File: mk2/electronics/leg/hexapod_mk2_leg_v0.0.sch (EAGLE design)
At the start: 5 parts

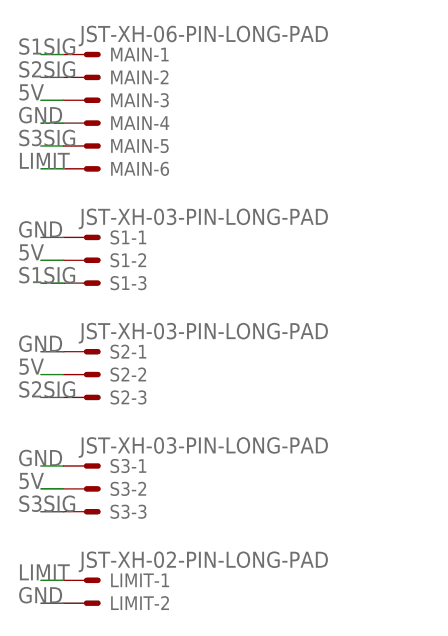
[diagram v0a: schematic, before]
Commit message: servo decoupling caps
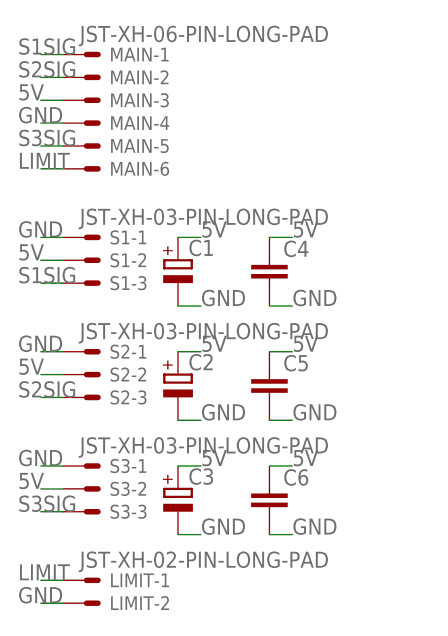
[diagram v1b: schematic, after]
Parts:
- added C1, C2, C3: (no value), rcl:CPOL-EUE2-5
- added C4, C5, C6: (no value), rcl:C-EUC1206
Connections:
- net 5V: now also C1.+, C2.+, C3.+, C4.1, C5.1, C6.1
- net GND: now also C1.-, C2.-, C3.-, C4.2, C5.2, C6.2
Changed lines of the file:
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@@
 <part name="LIMIT" library="Rembrandt Electronics - JST XH Connectors v1-0" deviceset="JST-XH-02-PIN" device="-LONG-PAD"/>
 <part name="MAIN" library="Rembrandt Electronics - JST XH Connectors v1-0" deviceset="JST-XH-06-PIN" device="-LONG-PAD"/>
+<part name="C1" library="rcl" library_urn="urn:adsk.eagle:library:334" deviceset="CPOL-EU" device="E2-5" package3d_urn="urn:adsk.eagle:package:23346/2"/>
+<part name="C2" library="rcl" library_urn="urn:adsk.eagle:library:334" deviceset="CPOL-EU" device="E2-5" package3d_urn="urn:adsk.eagle:package:23346/2"/>
+<part name="C3" library="rcl" library_urn="urn:adsk.eagle:library:334" deviceset="CPOL-EU" device="E2-5" package3d_urn="urn:adsk.eagle:package:23346/2"/>
+<part name="C4" library="rcl" library_urn="urn:adsk.eagle:library:334" deviceset="C-EU" device="C1206" package3d_urn="urn:adsk.eagle:package:23618/2"/>
+<part name="C5" library="rcl" library_urn="urn:adsk.eagle:library:334" deviceset="C-EU" device="C1206" package3d_urn="urn:adsk.eagle:package:23618/2"/>
+<part name="C6" library="rcl" library_urn="urn:adsk.eagle:library:334" deviceset="C-EU" device="C1206" package3d_urn="urn:adsk.eagle:package:23618/2"/>
 </parts>
 <sheets>
@@
 <attribute name="NAME" x="35.56" y="65.278" size="1.524" layer="95"/>
 </instance>
+<instance part="C1" gate="G$1" x="43.18" y="55.88" smashed="yes">
+<attribute name="NAME" x="44.323" y="56.3626" size="1.778" layer="95"/>
+<attribute name="VALUE" x="44.323" y="51.2826" size="1.778" layer="96"/>
+</instance>
+<instance part="C2" gate="G$1" x="43.18" y="43.18" smashed="yes">
+<attribute name="NAME" x="44.323" y="43.6626" size="1.778" layer="95"/>
+<attribute name="VALUE" x="44.323" y="38.5826" size="1.778" layer="96"/>
+</instance>
+<instance part="C3" gate="G$1" x="43.18" y="30.48" smashed="yes">
+<attribute name="NAME" x="44.323" y="30.9626" size="1.778" layer="95"/>
+<attribute name="VALUE" x="44.323" y="25.8826" size="1.778" layer="96"/>
+</instance>
+<instance part="C4" gate="G$1" x="53.34" y="55.88" smashed="yes">
+<attribute name="NAME" x="54.864" y="56.261" size="1.778" layer="95"/>
+<attribute name="VALUE" x="54.864" y="51.181" size="1.778" layer="96"/>
+</instance>
+<instance part="C5" gate="G$1" x="53.34" y="43.18" smashed="yes">
+<attribute name="NAME" x="54.864" y="43.561" size="1.778" layer="95"/>
+<attribute name="VALUE" x="54.864" y="38.481" size="1.778" layer="96"/>
+</instance>
+<instance part="C6" gate="G$1" x="53.34" y="30.48" smashed="yes">
+<attribute name="NAME" x="54.864" y="30.861" size="1.778" layer="95"/>
+<attribute name="VALUE" x="54.864" y="25.781" size="1.778" layer="96"/>
+</instance>
 </instances>
 <busses>
@@
 <label x="25.4" y="73.66" size="1.778" layer="95"/>
 </segment>
+<segment>
+<pinref part="C3" gate="G$1" pin="+"/>
+<wire x1="43.18" y1="33.02" x2="45.72" y2="33.02" width="0.1524" layer="91"/>
+<label x="45.72" y="33.02" size="1.778" layer="95"/>
+</segment>
+<segment>
+<pinref part="C2" gate="G$1" pin="+"/>
+<wire x1="43.18" y1="45.72" x2="45.72" y2="45.72" width="0.1524" layer="91"/>
+<label x="45.72" y="45.72" size="1.778" layer="95"/>
+</segment>
+<segment>
+<pinref part="C1" gate="G$1" pin="+"/>
+<wire x1="43.18" y1="58.42" x2="45.72" y2="58.42" width="0.1524" layer="91"/>
+<label x="45.72" y="58.42" size="1.778" layer="95"/>
+</segment>
+<segment>
+<pinref part="C4" gate="G$1" pin="1"/>
+<wire x1="53.34" y1="58.42" x2="55.88" y2="58.42" width="0.1524" layer="91"/>
+<label x="55.88" y="58.42" size="1.778" layer="95"/>
+</segment>
+<segment>
+<pinref part="C5" gate="G$1" pin="1"/>
+<wire x1="53.34" y1="45.72" x2="55.88" y2="45.72" width="0.1524" layer="91"/>
+<label x="55.88" y="45.72" size="1.778" layer="95"/>
+</segment>
+<segment>
+<pinref part="C6" gate="G$1" pin="1"/>
+<wire x1="53.34" y1="33.02" x2="55.88" y2="33.02" width="0.1524" layer="91"/>
+<label x="55.88" y="33.02" size="1.778" layer="95"/>
+</segment>
 </net>
 <net name="GND" class="0">
@@
 <label x="25.4" y="71.12" size="1.778" layer="95"/>
 </segment>
+<segment>
+<pinref part="C3" gate="G$1" pin="-"/>
+<wire x1="43.18" y1="25.4" x2="45.72" y2="25.4" width="0.1524" layer="91"/>
+<label x="45.72" y="25.4" size="1.778" layer="95"/>
+</segment>
+<segment>
+<pinref part="C2" gate="G$1" pin="-"/>
+<wire x1="43.18" y1="38.1" x2="45.72" y2="38.1" width="0.1524" layer="91"/>
+<label x="45.72" y="38.1" size="1.778" layer="95"/>
+</segment>
+<segment>
+<pinref part="C1" gate="G$1" pin="-"/>
+<wire x1="43.18" y1="50.8" x2="45.72" y2="50.8" width="0.1524" layer="91"/>
+<label x="45.72" y="50.8" size="1.778" layer="95"/>
+</segment>
+<segment>
+<pinref part="C6" gate="G$1" pin="2"/>
+<wire x1="53.34" y1="25.4" x2="55.88" y2="25.4" width="0.1524" layer="91"/>
+<label x="55.88" y="25.4" size="1.778" layer="95"/>
+</segment>
+<segment>
+<pinref part="C5" gate="G$1" pin="2"/>
+<wire x1="53.34" y1="38.1" x2="55.88" y2="38.1" width="0.1524" layer="91"/>
+<label x="55.88" y="38.1" size="1.778" layer="95"/>
+</segment>
+<segment>
+<pinref part="C4" gate="G$1" pin="2"/>
+<wire x1="53.34" y1="50.8" x2="55.88" y2="50.8" width="0.1524" layer="91"/>
+<label x="55.88" y="50.8" size="1.778" layer="95"/>
+</segment>
 </net>
 <net name="S1SIG" class="0">
@@
 </sheet>
 </sheets>
+<errors>
+</errors>
 </schematic>
 </drawing>
+<compatibility>
+<note version="8.2" severity="warning">
+Since Version 8.2, EAGLE supports online libraries. The ids
+of those online libraries will not be understood (or retained)
+with this version.
+</note>
+<note version="8.3" severity="warning">
+Since Version 8.3, EAGLE supports URNs for individual library
+assets (packages, symbols, and devices). The URNs of those assets
+will not be understood (or retained) with this version.
+</note>
+<note version="8.3" severity="warning">
+Since Version 8.3, EAGLE supports the association of 3D packages
+with devices in libraries, schematics, and board files. Those 3D
+packages will not be understood (or retained) with this version.
+</note>
+<note version="8.4" severity="warning">
+Since Version 8.4, EAGLE supports properties for SPICE simulation.
+Probes in schematics and SPICE mapping objects found in parts and library devices
+will not be understood with this version. Update EAGLE to the latest version
+for full support of SPICE simulation.
+</note>
+</compatibility>
 </eagle>
